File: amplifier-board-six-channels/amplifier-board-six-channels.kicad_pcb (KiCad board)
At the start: 2 copper layers, 50 x 45 mm, 93 parts, among them J1 Conn_02x08_Odd_Even, J2 Conn_02x08_Odd_Even, U1 Opamp_Dual, U2 Opamp_Dual, U3 Opamp_Dual, U4 Opamp_Dual, U5 Opamp_Dual, U6 Opamp_Dual, U7 MAX6035xxUR25

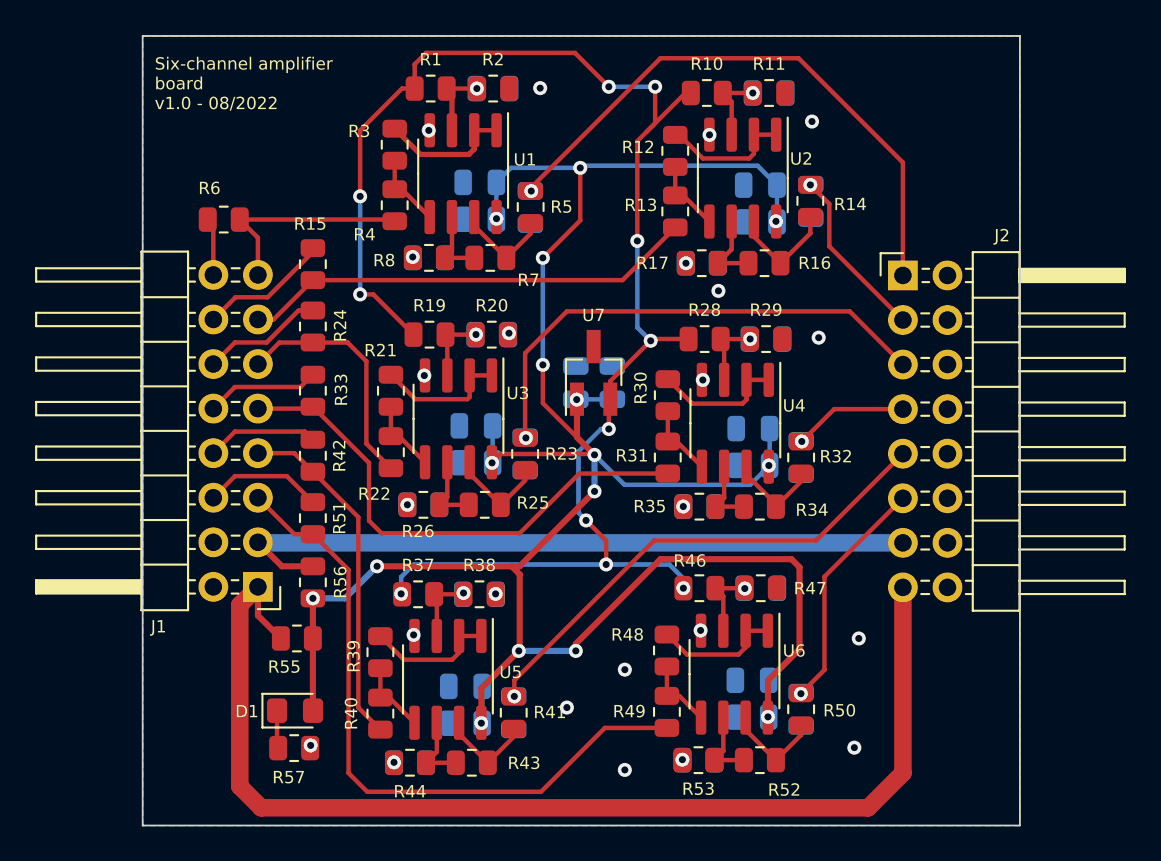
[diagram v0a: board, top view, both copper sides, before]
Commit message: Updated boards with dates, silk, mounting holes
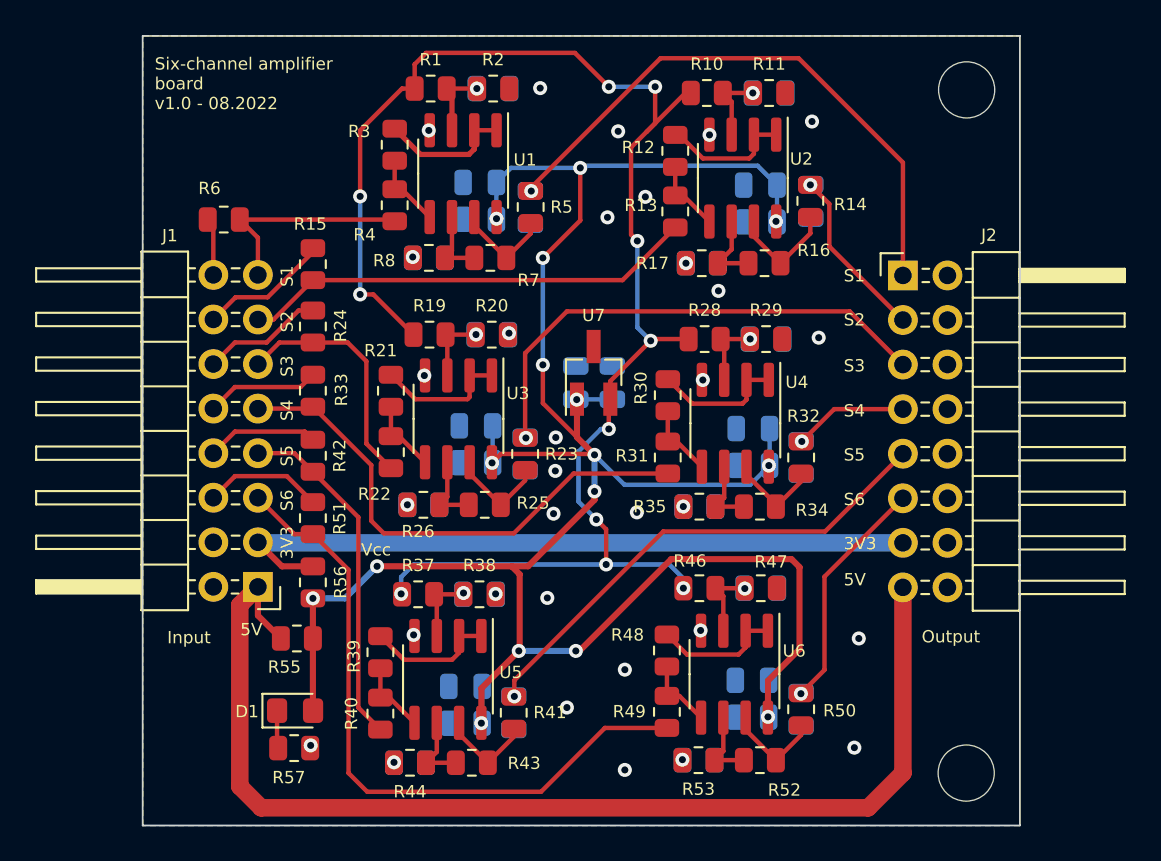
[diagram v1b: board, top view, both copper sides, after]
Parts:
- added REF**: MountingHole_3.2mm_M3, MountingHole:MountingHole_3.2mm_M3, F.Cu at (80.7, 20.5)
- added REF**: MountingHole_3.2mm_M3, MountingHole:MountingHole_3.2mm_M3, F.Cu at (80.7, 59.5)
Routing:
- net GND: vias 18 -> 26
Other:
- board text added: "3V3"
- board text added: "5V"
- board text added: "Input"
- board text added: "Output"
- board text added: "S1"
- board text added: "S2"
- board text added: "S3"
- board text added: "S4"
- board text added: "S5"
- board text added: "S6"
- board text added: "Six-channel amplifier board v1.0 - 08.2022"
- board text added: "Vcc"
- board text removed: "Six-channel amplifier board v1.0 - 08/2022"
